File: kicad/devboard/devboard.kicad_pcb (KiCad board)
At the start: 2 copper layers, 34.5 x 25 mm, 34 parts, among them J1 USB_C_Receptacle, J2 Conn_02x02_Top_Bottom, J3 Conn_01x04_Socket, U1 LM3940, U2 CH340G, U3 STM32G030K8Tx, Y1 12 MHz, Y2 8 MHz

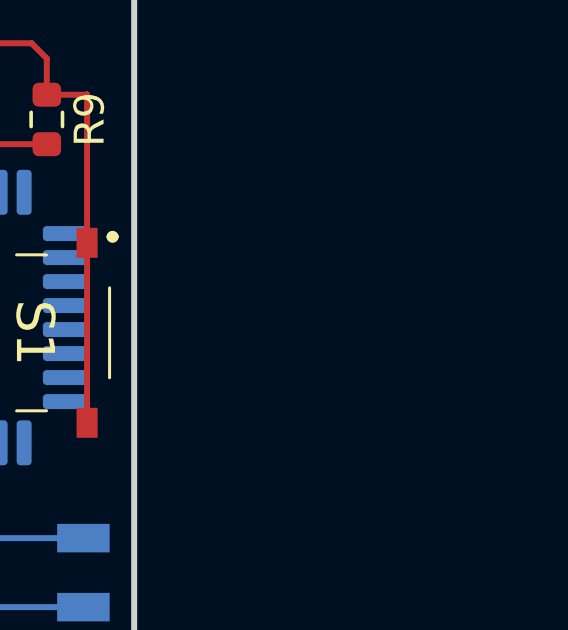
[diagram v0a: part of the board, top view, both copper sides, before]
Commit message: integrated and added transistor to pcb
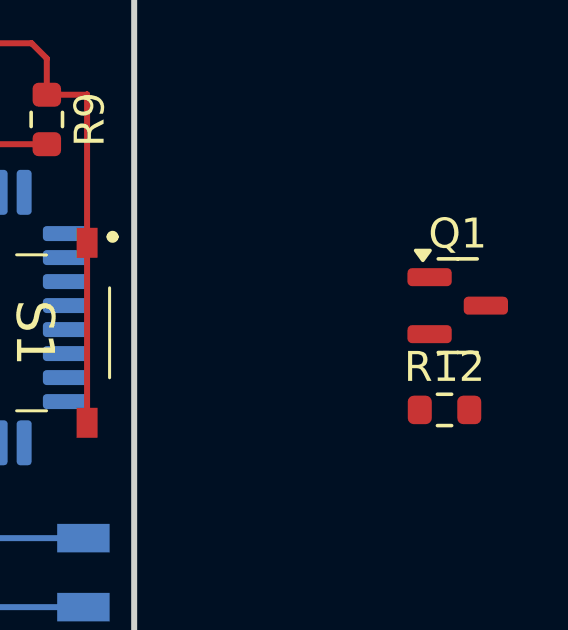
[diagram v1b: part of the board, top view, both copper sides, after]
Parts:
- added Q1: BSS138, Package_TO_SOT_SMD:SOT-23, F.Cu at (146.3, 60.1)
- added R12: 10k, Resistor_SMD:R_0603_1608Metric, F.Cu at (145.8, 63.5)
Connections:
- U3 pad 7: Net-(D2-DIN) -> Net-(Q1-G)

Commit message: reconfigured slightly
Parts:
- C7, Q1, R12: moved to B.Cu
- R2, R3, R4, R8: moved to F.Cu
- moved R6 19.0 mm to (122.0, 57.2), turned to 90 degrees
- moved R5 17.5 mm to (119.7, 57.2), turned to 90 degrees
- moved Q1 17.0 mm to (133.6, 71.4), turned to 90 degrees
- moved R7 13.9 mm to (116.5, 68.1)
- moved R12 13.7 mm to (132.7, 67.3), turned to 90 degrees
- moved C3 11.4 mm to (108.7, 66.8)
- moved C2 11.1 mm to (118.5, 64.8), turned to -90 degrees
- moved R8 8.82 mm to (113.0, 69.3), turned to -90 degrees
- moved Y2 7.41 mm to (120.0, 64.0)
- moved R1 6.97 mm to (103.2, 67.5)
- moved D4 5.87 mm to (117.2, 66.5), turned to 0 degrees
- moved U2 5.41 mm to (114.0, 60.9), turned to 180 degrees
- moved D1 5.32 mm to (111.1, 51.1), turned to 90 degrees
- moved TH1 4.82 mm to (103.9, 50.6)
- moved U1 3.51 mm to (127.2, 69.9)
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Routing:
- net +5V: track 20.1 -> 59.0 mm
- net GND: track 26.6 -> 2.64 mm, vias 1 -> 0
- net Net-(J1-SHIELD): track 0.00 -> 19.3 mm
- net Net-(J1-VBUS-PadA4): track 0.00 -> 18.0 mm, vias 0 -> 2
- net Net-(U2-XI): track 0.00 -> 16.9 mm
- net Net-(D2-DIN): track 0.00 -> 15.1 mm, vias 0 -> 1
- net Net-(U2-UD+): track 0.00 -> 13.1 mm, vias 0 -> 1
- net Net-(U2-UD-): track 0.00 -> 12.1 mm, vias 0 -> 1
- net Net-(U2-XO): track 0.00 -> 11.0 mm
- net Net-(Q1-G): track 0.00 -> 10.9 mm
- net /RESET: track 0.00 -> 9.12 mm
- net Net-(D2-DOUT): track 0.00 -> 6.01 mm
- net Net-(D4-K): track 0.00 -> 4.16 mm
- net +3.3V: track 22.0 -> 24.6 mm
- net Net-(J1-CC1): track 0.00 -> 1.99 mm
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
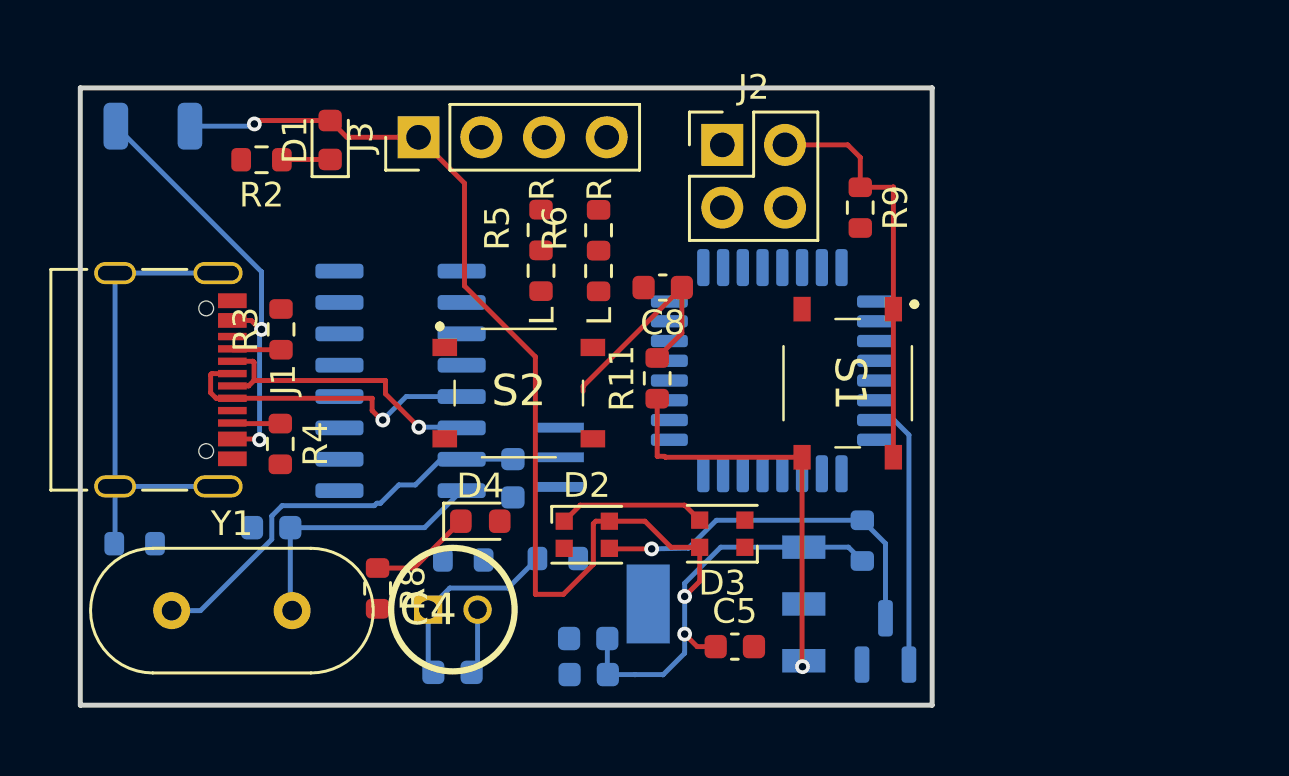
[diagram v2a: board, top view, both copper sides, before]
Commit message: mostly routed
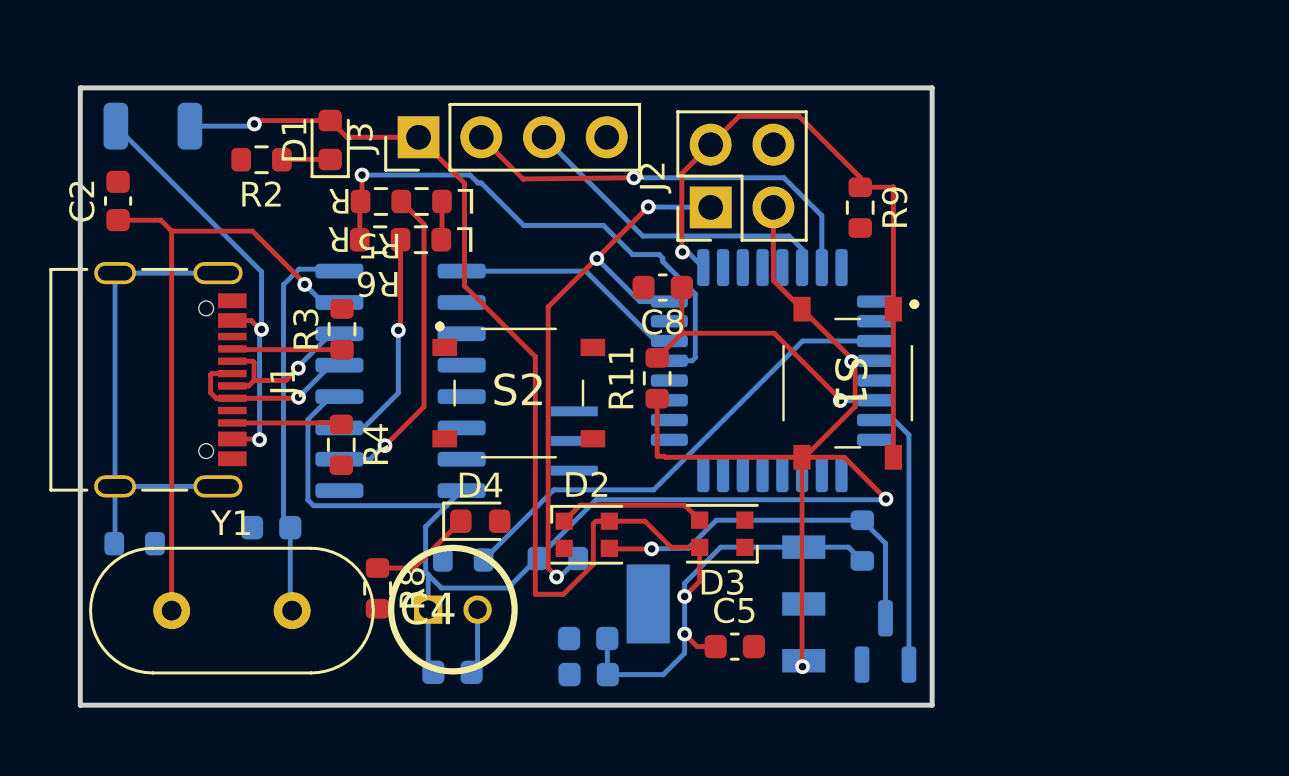
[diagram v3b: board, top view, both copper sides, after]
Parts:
- C2: moved to F.Cu
- moved C2 19.5 mm to (102.5, 53.6), turned to 90 degrees
- moved R6 6.70 mm to (115.6, 55.1), turned to 180 degrees
- moved R5 5.41 mm to (115.7, 53.6), turned to 180 degrees
- moved J2 2.58 mm to (126.5, 53.8), turned to 90 degrees
- moved R4 2.47 mm to (111.6, 63.5)
- moved R3 2.47 mm to (111.6, 58.8)
- moved Y2 0.87 mm to (120.6, 63.3)
- turned U2 to 0 degrees
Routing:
- net +3.3V: track 24.6 -> 73.5 mm, vias 1 -> 3
- net /SWDIO: track 0.00 -> 24.4 mm, vias 0 -> 3
- net /RX-M: track 0.00 -> 21.9 mm, vias 0 -> 1
- net Net-(U3-PC15): track 0.00 -> 19.5 mm
- net /I2C1_SDA: track 0.00 -> 17.3 mm, vias 0 -> 1
- net /TX-U: track 0.00 -> 13.1 mm, vias 0 -> 1
- net /I2C1_SCL: track 0.00 -> 13.1 mm
- net Net-(U2-~{CTS}): track 0.00 -> 9.59 mm
- net /SWCLK/BOOT: track 16.8 -> 26.2 mm, vias 0 -> 1
- net /RX-U: track 0.00 -> 9.32 mm, vias 0 -> 1
- net Net-(U2-XI): track 16.9 -> 25.8 mm, vias 0 -> 1
- net Net-(U2-UD+): track 13.1 -> 7.49 mm
- net Net-(U2-UD-): track 12.1 -> 6.89 mm
- net Net-(U2-XO): track 11.0 -> 15.9 mm
- net /RESET: track 9.12 -> 12.4 mm, vias 0 -> 1
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
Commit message: ROUTED!!!!
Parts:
- moved R11 0.87 mm to (124.3, 61.6)
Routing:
- net Net-(U2-~{RTS}): track 0.00 -> 15.9 mm, vias 0 -> 2
- net Net-(U3-PC14): track 0.00 -> 15.0 mm, vias 0 -> 2
- net /STATUS: track 0.00 -> 14.5 mm, vias 0 -> 1
- net /RESET: track 12.4 -> 25.4 mm, vias 1 -> 3
- net /TX-M: track 1.56 -> 14.3 mm, vias 0 -> 3
- net Net-(R7-Pad2): track 0.00 -> 6.82 mm
- net +3.3V: track 73.5 -> 72.4 mm

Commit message: Updated fresh layout of pieces
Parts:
- C2: moved to B.Cu
- moved TH1 20.8 mm to (108.0, 71.0)
- moved C6 19.2 mm to (132.7, 63.0), turned to 180 degrees
- moved R5 18.9 mm to (107.3, 70.5)
- moved R6 18.9 mm to (107.3, 72.0)
- moved Y1 18.2 mm to (104.5, 52.0)
- moved R7 18.1 mm to (132.7, 60.0), turned to 0 degrees
- moved C3 14.5 mm to (112.0, 52.7), turned to -90 degrees
- moved Y2 13.1 mm to (132.1, 57.0)
- moved D1 6.42 mm to (115.3, 56.0), turned to 0 degrees
- moved R9 5.82 mm to (127.4, 56.4), turned to 180 degrees
- moved S1 5.04 mm to (132.1, 66.0)
- moved R2 4.80 mm to (110.8, 56.0)
- moved C2 4.55 mm to (107.0, 52.7), turned to -90 degrees
- moved U3 4.06 mm to (125.0, 60.0)
- moved J2 3.98 mm to (130.5, 53.5)
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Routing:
- net +5V: track 58.9 -> 17.9 mm, vias 3 -> 2
- net /SWCLK/BOOT: track 26.2 -> 0.00 mm, vias 1 -> 0
- net Net-(U2-XI): track 25.8 -> 0.00 mm, vias 1 -> 0
- net /SWDIO: track 24.2 -> 0.00 mm, vias 3 -> 0
- net /RX-M: track 21.9 -> 0.00 mm, vias 1 -> 0
- net /RESET: track 25.4 -> 5.47 mm, vias 3 -> 0
- net Net-(U3-PC15): track 19.5 -> 0.00 mm
- net +3.3V: track 72.4 -> 54.8 mm, vias 3 -> 2
- net /I2C1_SDA: track 17.3 -> 0.00 mm, vias 1 -> 0
- net Net-(U2-~{RTS}): track 15.9 -> 0.00 mm, vias 2 -> 0
- net Net-(U2-XO): track 15.9 -> 0.00 mm
- net Net-(U3-PC14): track 15.0 -> 0.10 mm, vias 2 -> 0
- net /STATUS: track 14.5 -> 0.00 mm, vias 1 -> 0
- net /TX-M: track 14.3 -> 0.00 mm, vias 3 -> 0
- net /I2C1_SCL: track 13.1 -> 0.00 mm
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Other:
- rule pad_to_mask_clearance: 0 -> 0.0508

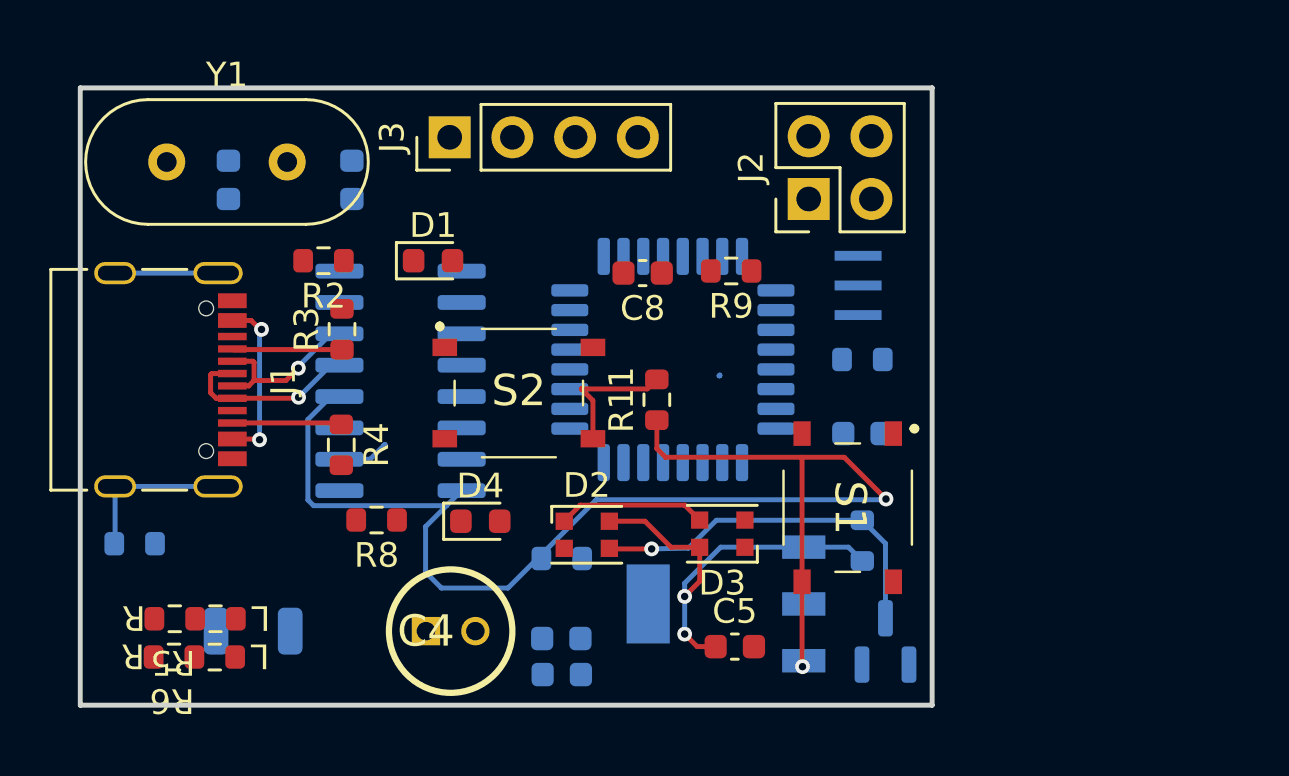
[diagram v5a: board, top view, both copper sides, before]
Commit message: Added most routing, besides the debug header
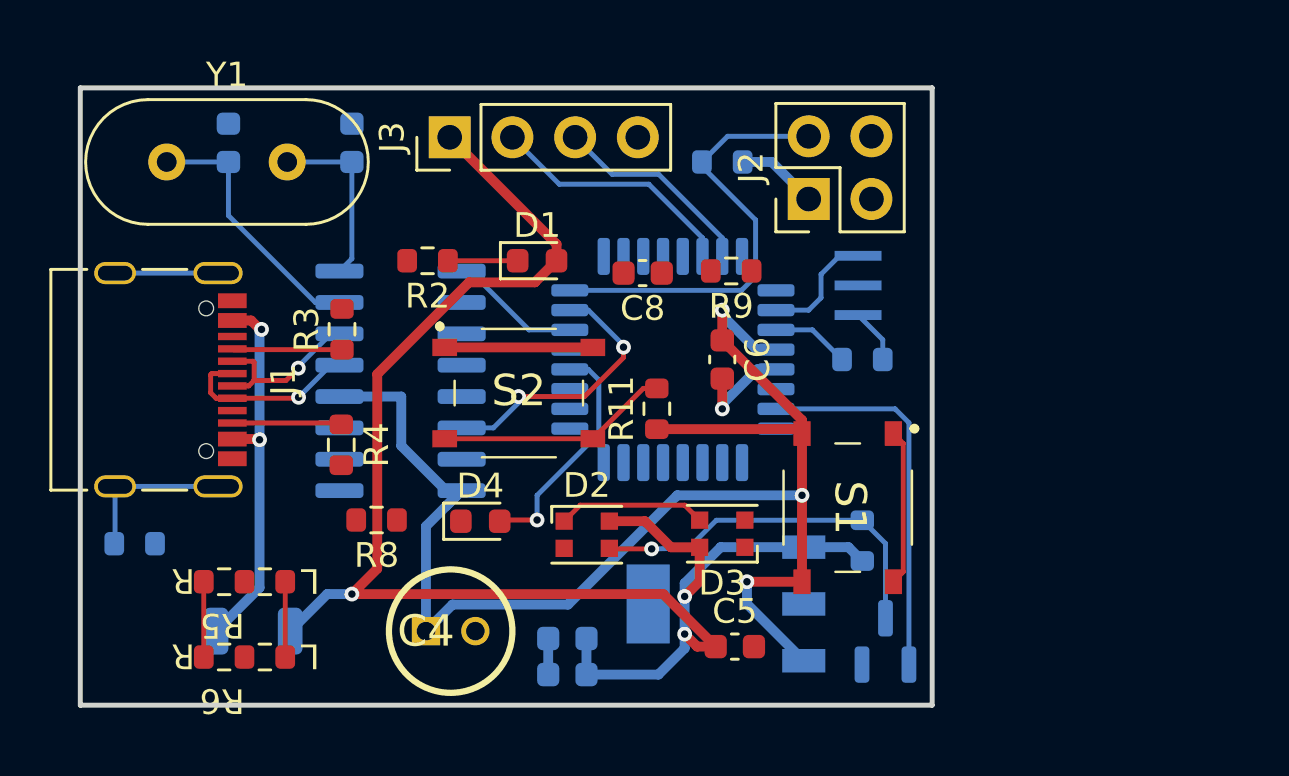
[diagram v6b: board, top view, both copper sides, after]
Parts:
- C6: moved to F.Cu
- moved R10 17.3 mm to (127.0, 52.0), turned to 180 degrees
- moved C6 6.42 mm to (127.0, 60.0), turned to -90 degrees
- moved D1 4.21 mm to (119.5, 56.0)
- moved R2 4.21 mm to (115.1, 56.0)
- moved R5 2.50 mm to (109.3, 69.0)
- moved R6 2.03 mm to (109.3, 72.0)
- moved C2 1.50 mm to (107.0, 51.2), turned to 90 degrees
- moved C3 1.50 mm to (112.0, 51.2), turned to 90 degrees
- moved R11 0.36 mm to (124.3, 62.0)
- moved C1 0.24 mm to (120.7, 71.3)
- moved C7 0.22 mm to (120.7, 72.8)
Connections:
- J2 pad 1: /SWDIO -> +3.3V
- J2 pad 2: /SWCLK/BOOT -> /SWDIO
- J2 pad 3: +3.3V -> GND
- J2 pad 4: GND -> /SWCLK/BOOT
- J3 pad 2: /I2C1_SDA -> /I2C1_SCL
- J3 pad 3: /I2C1_SCL -> /I2C1_SDA
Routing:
- net +5V: track 17.9 -> 68.4 mm, vias 2 -> 3
- net /SWDIO: track 0.00 -> 18.0 mm
- net Net-(Q1-G): track 0.00 -> 15.4 mm
- net GND: track 0.00 -> 11.6 mm, vias 0 -> 1
- net Net-(U2-~{RTS}): track 0.00 -> 11.1 mm, vias 0 -> 2
- net Net-(U2-XI): track 0.00 -> 10.6 mm
- net /I2C1_SCL: track 0.00 -> 10.1 mm
- net /STATUS: track 0.00 -> 9.59 mm, vias 0 -> 1
- net +3.3V: track 54.8 -> 63.6 mm, vias 2 -> 3
- net Net-(J1-VBUS-PadA4): track 7.35 -> 15.8 mm
- net /I2C1_SDA: track 0.00 -> 8.40 mm
- net Net-(U2-XO): track 0.00 -> 7.25 mm
- net /SWCLK/BOOT: track 0.00 -> 6.33 mm
- net Net-(U2-~{CTS}): track 0.00 -> 5.37 mm
- net Net-(U3-PC14): track 0.10 -> 4.79 mm
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
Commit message: routed remaining components
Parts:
- moved S2 14.5 mm to (108.0, 71.0)
- moved R5 10.3 mm to (118.1, 63.6), turned to 90 degrees
- moved R6 10.2 mm to (115.1, 63.6), turned to 90 degrees
- moved R9 0.58 mm to (127.1, 55.9)
- moved C6 0.58 mm to (127.4, 59.6)
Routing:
- net /SWCLK/BOOT: track 6.33 -> 40.3 mm, vias 0 -> 3
- net /RESET: track 9.43 -> 37.1 mm, vias 0 -> 3
- net +3.3V: track 63.6 -> 75.2 mm, vias 3 -> 4
- net /TX-U: track 0.00 -> 11.5 mm, vias 0 -> 1
- net Net-(J1-SHIELD): track 10.7 -> 19.3 mm
- net Net-(U2-~{RTS}): track 11.1 -> 17.7 mm, vias 2 -> 0
- net /TX-M: track 3.05 -> 7.28 mm, vias 0 -> 1
- net /RX-U: track 0.00 -> 3.89 mm, vias 0 -> 1
- net /RX-M: track 3.05 -> 6.91 mm, vias 0 -> 1
- net Net-(D4-K): track 0.00 -> 2.61 mm
- net /SWDIO: track 18.0 -> 16.3 mm, vias 0 -> 2
- net GND: track 11.6 -> 10.2 mm
- net +5V: track 68.4 -> 67.6 mm, vias 3 -> 4

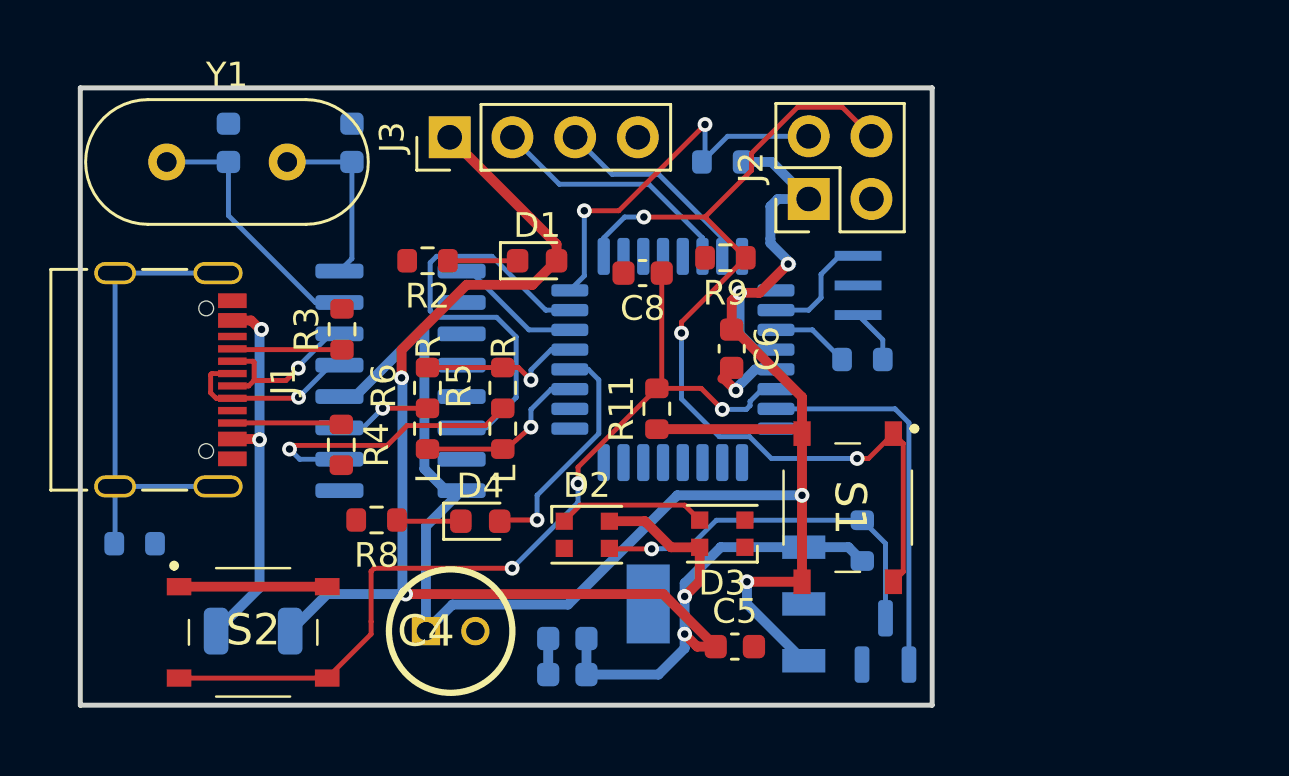
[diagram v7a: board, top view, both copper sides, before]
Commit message: Fixed USB routing, simplified other routes
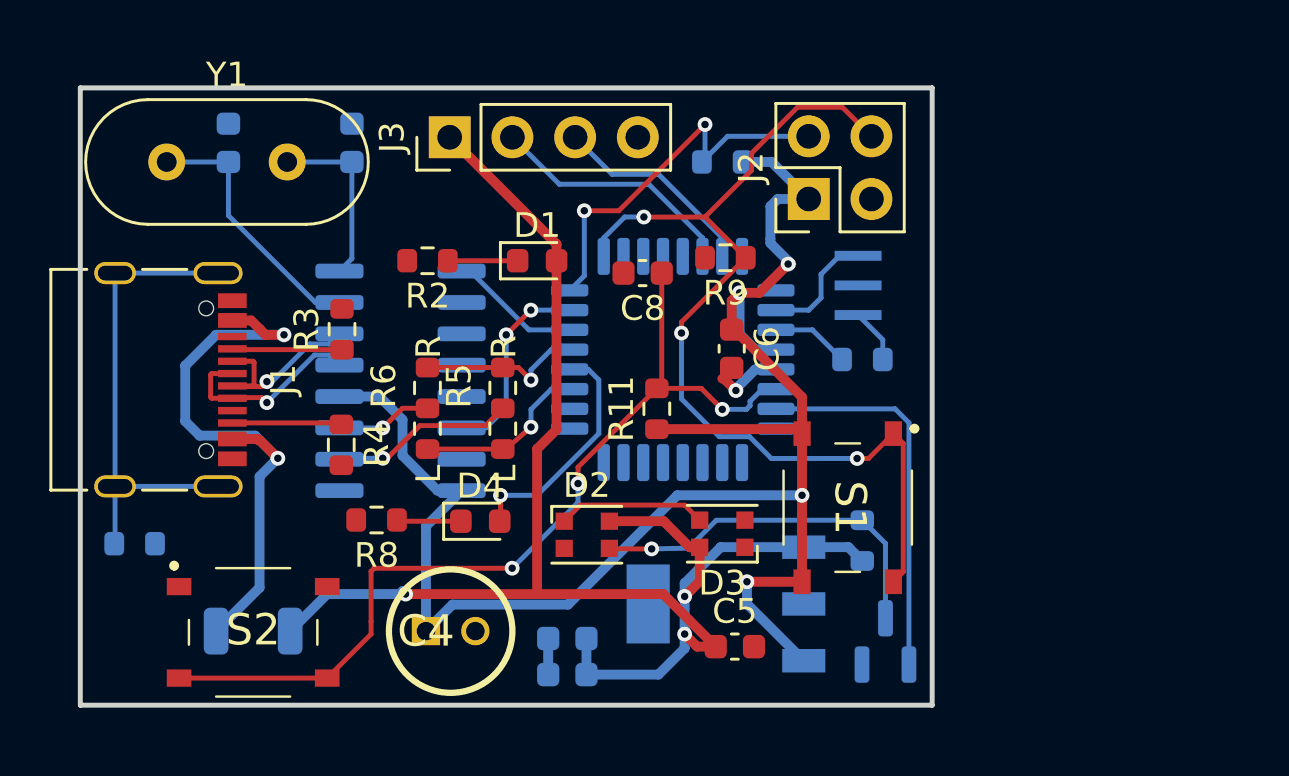
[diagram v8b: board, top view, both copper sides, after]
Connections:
- net Net-(U2-UD+) renamed /USBD+
- net Net-(U2-UD-) renamed /USBD-
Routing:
- net Net-(U2-~{RTS}): track 17.7 -> 8.08 mm, vias 0 -> 2
- net Net-(J1-VBUS-PadA4): track 15.8 -> 23.8 mm
- net GND: track 10.2 -> 4.23 mm
- net +3.3V: track 75.2 -> 70.4 mm
- net /TX-U: track 11.5 -> 7.47 mm
- net +5V: track 67.6 -> 63.9 mm, vias 4 -> 3
- net /USBD-: track 6.89 -> 7.93 mm
- net /USBD+: track 7.49 -> 8.10 mm
